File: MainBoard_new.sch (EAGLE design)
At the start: 60 parts, among them T1 BC847, U1 STM32F10XRXT6, Y1 8MHz, Y2 32.768kHz

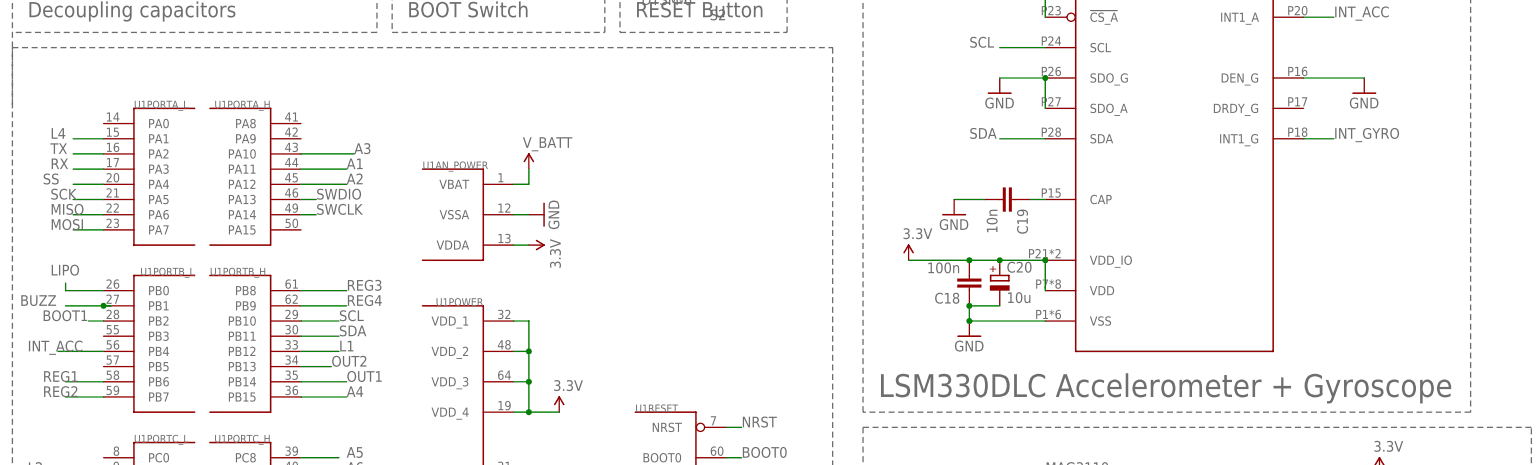
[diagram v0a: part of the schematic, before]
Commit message: odczyt z czujników
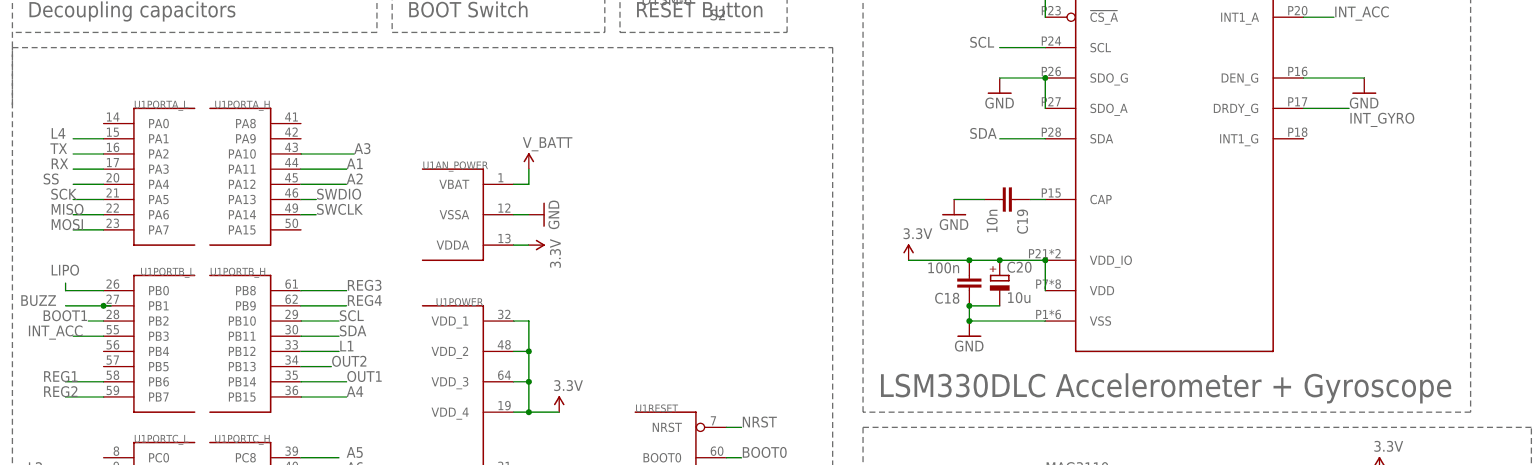
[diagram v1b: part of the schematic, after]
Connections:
- net INT_ACC: now also U1PORTB_L.PB3; no longer U1PORTB_L.PB4
- net INT_GYRO: now also LSM330DLC.DRDY_G; no longer LSM330DLC.INT1_G
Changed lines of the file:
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@@
 </segment>
 <segment>
-<pinref part="U1" gate="PORTB_L" pin="PB4"/>
-<wire x1="15.24" y1="50.8" x2="7.62" y2="50.8" width="0.1524" layer="91"/>
-<label x="2.54" y="50.8" size="1.778" layer="95"/>
+<pinref part="U1" gate="PORTB_L" pin="PB3"/>
+<wire x1="15.24" y1="53.34" x2="10.16" y2="53.34" width="0.1524" layer="91"/>
+<label x="2.54" y="53.34" size="1.778" layer="95"/>
 </segment>
 </net>
 <net name="INT_GYRO" class="0">
-<segment>
-<pinref part="LSM330DLC" gate="G$1" pin="INT1_G"/>
-<wire x1="215.9" y1="86.36" x2="220.98" y2="86.36" width="0.1524" layer="91"/>
-<label x="220.98" y="86.36" size="1.778" layer="95"/>
-</segment>
 <segment>
 <pinref part="U1" gate="PORTC_L" pin="PC5"/>
@@
 <label x="2.54" y="20.32" size="1.778" layer="95"/>
 </segment>
+<segment>
+<pinref part="LSM330DLC" gate="G$1" pin="DRDY_G"/>
+<wire x1="215.9" y1="91.44" x2="223.52" y2="91.44" width="0.1524" layer="91"/>
+<label x="223.52" y="88.9" size="1.778" layer="95"/>
+</segment>
 </net>

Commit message: poprawki płytki, kodzik
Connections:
- net 5V: now also JP5.2, JP6.2, JP7.2, JP8.2; no longer JP5.1, JP6.1, JP7.1, JP8.1
- net GND: now also JP5.1, JP6.1, JP7.1, JP8.1; no longer JP5.2, JP6.2, JP7.2, JP8.2
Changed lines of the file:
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@@
-</segment>
-<segment>
-<pinref part="JP5" gate="G$1" pin="2"/>
-<wire x1="121.92" y1="205.74" x2="127" y2="205.74" width="0.1524" layer="91"/>
-<label x="127" y="205.74" size="1.778" layer="95"/>
-</segment>
-<segment>
-<pinref part="JP6" gate="G$1" pin="2"/>
-<wire x1="121.92" y1="191.77" x2="127" y2="191.77" width="0.1524" layer="91"/>
-<label x="127" y="191.77" size="1.778" layer="95"/>
-</segment>
-<segment>
-<pinref part="JP7" gate="G$1" pin="2"/>
-<wire x1="123.19" y1="179.07" x2="128.27" y2="179.07" width="0.1524" layer="91"/>
-<label x="128.27" y="179.07" size="1.778" layer="95"/>
-</segment>
-<segment>
-<pinref part="JP8" gate="G$1" pin="2"/>
-<wire x1="124.46" y1="165.1" x2="129.54" y2="165.1" width="0.1524" layer="91"/>
-<label x="129.54" y="165.1" size="1.778" layer="95"/>
 </segment>
 <segment>
@@
 <junction x="177.8" y="162.56"/>
 </segment>
+<segment>
+<pinref part="JP6" gate="G$1" pin="1"/>
+<wire x1="121.92" y1="189.23" x2="127" y2="189.23" width="0.1524" layer="91"/>
+<label x="127" y="189.23" size="1.778" layer="95"/>
+</segment>
+<segment>
+<pinref part="JP7" gate="G$1" pin="1"/>
+<wire x1="123.19" y1="176.53" x2="128.27" y2="176.53" width="0.1524" layer="91"/>
+<label x="128.27" y="176.53" size="1.778" layer="95"/>
+</segment>
+<segment>
+<pinref part="JP8" gate="G$1" pin="1"/>
+<wire x1="124.46" y1="162.56" x2="129.54" y2="162.56" width="0.1524" layer="91"/>
+<label x="129.54" y="162.56" size="1.778" layer="95"/>
+</segment>
+<segment>
+<pinref part="JP5" gate="G$1" pin="1"/>
+<wire x1="121.92" y1="203.2" x2="127" y2="203.2" width="0.1524" layer="91"/>
+<label x="127" y="203.2" size="1.778" layer="95"/>
+</segment>
 </net>
 <net name="SWDIO" class="0">
@@
 <net name="5V" class="0">
 <segment>
-<pinref part="JP5" gate="G$1" pin="1"/>
-<wire x1="121.92" y1="203.2" x2="127" y2="203.2" width="0.1524" layer="91"/>
-<label x="127" y="203.2" size="1.778" layer="95"/>
-</segment>
-<segment>
-<pinref part="JP6" gate="G$1" pin="1"/>
-<wire x1="121.92" y1="189.23" x2="127" y2="189.23" width="0.1524" layer="91"/>
-<label x="127" y="189.23" size="1.778" layer="95"/>
-</segment>
-<segment>
-<pinref part="JP7" gate="G$1" pin="1"/>
-<wire x1="123.19" y1="176.53" x2="128.27" y2="176.53" width="0.1524" layer="91"/>
-<label x="128.27" y="176.53" size="1.778" layer="95"/>
-</segment>
-<segment>
-<pinref part="JP8" gate="G$1" pin="1"/>
-<wire x1="124.46" y1="162.56" x2="129.54" y2="162.56" width="0.1524" layer="91"/>
-<label x="129.54" y="162.56" size="1.778" layer="95"/>
-</segment>
-<segment>
 <pinref part="JP9" gate="G$1" pin="1"/>
 <wire x1="119.38" y1="223.52" x2="127" y2="223.52" width="0.1524" layer="91"/>
 <label x="127" y="223.52" size="1.778" layer="95"/>
 </segment>
-</net>
+<segment>
+<pinref part="JP5" gate="G$1" pin="2"/>
+<wire x1="121.92" y1="205.74" x2="127" y2="205.74" width="0.1524" layer="91"/>
+<label x="127" y="205.74" size="1.778" layer="95"/>
+</segment>
+<segment>
+<pinref part="JP6" gate="G$1" pin="2"/>
+<wire x1="121.92" y1="191.77" x2="127" y2="191.77" width="0.1524" layer="91"/>
+<label x="127" y="191.77" size="1.778" layer="95"/>
+</segment>
+<segment>
+<pinref part="JP7" gate="G$1" pin="2"/>
+<wire x1="123.19" y1="179.07" x2="128.27" y2="179.07" width="0.1524" layer="91"/>
+<label x="128.27" y="179.07" size="1.778" layer="95"/>
+</segment>
+<segment>
+<pinref part="JP8" gate="G$1" pin="2"/>
+<wire x1="124.46" y1="165.1" x2="129.54" y2="165.1" width="0.1524" layer="91"/>
+<label x="129.54" y="165.1" size="1.778" layer="95"/>
+</segment>
+</net>
